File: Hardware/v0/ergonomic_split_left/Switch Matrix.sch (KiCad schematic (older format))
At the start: 86 parts, among them SW100 L41, SW101 L51, SW102 L02, SW103 L12, SW104 L22, SW105 L32, SW106 L42, SW107 L52, SW108 L03, SW109 L13, SW110 L23, SW111 L33, SW112 L43, SW113 L53, SW114 L04, SW115 L14, SW116 L24, SW117 L34, SW118 L44, SW119 L54, SW120 L05, SW121 L15, SW122 L25, SW123 L25, SW124 L55, SW125 L06, SW126 L16, SW127 L36, SW128 L56, SW90 L00, SW91 L10, SW92 L20, SW94 L30, SW95 L40, SW96 L01, SW97 L11, SW98 L21, SW99 L31

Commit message: Switch matrix placement
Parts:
- removed D1, D10, D11, D12, D120, D121, D122, D123, D124, D125, D126, D13, D14, D15, D16, D17, D18, D19, D2, D20, D21, D22, D23, D24, D25, D26, D27, D28, D29, D3, D30, D31, D4, D5, D6, D7, D8, D9: D, custom_footprint_library:SOD323_HS, symbol Device:D
- removed SW100: L41, CherryMX_PCB_KailhSocket:CherryMX_1.00u_PCB_KailhSocket, symbol CherryMX:CherryMX
- removed SW101: L51, CherryMX_PCB_KailhSocket:CherryMX_1.00u_PCB_KailhSocket, symbol CherryMX:CherryMX
- removed SW102: L02, CherryMX_PCB_KailhSocket:CherryMX_1.00u_PCB_KailhSocket, symbol CherryMX:CherryMX
- removed SW103: L12, CherryMX_PCB_KailhSocket:CherryMX_1.00u_PCB_KailhSocket, symbol CherryMX:CherryMX
- removed SW104: L22, CherryMX_PCB_KailhSocket:CherryMX_1.00u_PCB_KailhSocket, symbol CherryMX:CherryMX
- removed SW105: L32, CherryMX_PCB_KailhSocket:CherryMX_1.00u_PCB_KailhSocket, symbol CherryMX:CherryMX
- removed SW106: L42, CherryMX_PCB_KailhSocket:CherryMX_1.00u_PCB_KailhSocket, symbol CherryMX:CherryMX
- removed SW107: L52, CherryMX_PCB_KailhSocket:CherryMX_2.00u_PCB_KailhSocket, symbol CherryMX:CherryMX
- removed SW108: L03, CherryMX_PCB_KailhSocket:CherryMX_1.00u_PCB_KailhSocket, symbol CherryMX:CherryMX
- removed SW109: L13, CherryMX_PCB_KailhSocket:CherryMX_1.00u_PCB_KailhSocket, symbol CherryMX:CherryMX
- removed SW110: L23, CherryMX_PCB_KailhSocket:CherryMX_1.00u_PCB_KailhSocket, symbol CherryMX:CherryMX
- removed SW111: L33, CherryMX_PCB_KailhSocket:CherryMX_1.00u_PCB_KailhSocket, symbol CherryMX:CherryMX
- removed SW112: L43, CherryMX_PCB_KailhSocket:CherryMX_1.00u_PCB_KailhSocket, symbol CherryMX:CherryMX
- removed SW113: L53, CherryMX_PCB_KailhSocket:CherryMX_2.00u_PCB_KailhSocket, symbol CherryMX:CherryMX
- removed SW114: L04, CherryMX_PCB_KailhSocket:CherryMX_1.00u_PCB_KailhSocket, symbol CherryMX:CherryMX
- removed SW115: L14, CherryMX_PCB_KailhSocket:CherryMX_1.00u_PCB_KailhSocket, symbol CherryMX:CherryMX
- removed SW116: L24, CherryMX_PCB_KailhSocket:CherryMX_1.00u_PCB_KailhSocket, symbol CherryMX:CherryMX
- removed SW117: L34, CherryMX_PCB_KailhSocket:CherryMX_1.00u_PCB_KailhSocket, symbol CherryMX:CherryMX
- removed SW118: L44, CherryMX_PCB_KailhSocket:CherryMX_1.00u_PCB_KailhSocket, symbol CherryMX:CherryMX
- removed SW119: L54, CherryMX_PCB_KailhSocket:CherryMX_1.00u_PCB_KailhSocket, symbol CherryMX:CherryMX
- removed SW120: L05, CherryMX_PCB_KailhSocket:CherryMX_1.00u_PCB_KailhSocket, symbol CherryMX:CherryMX
- removed SW121: L15, CherryMX_PCB_KailhSocket:CherryMX_1.00u_PCB_KailhSocket, symbol CherryMX:CherryMX
- removed SW122, SW123: L25, CherryMX_PCB_KailhSocket:CherryMX_1.00u_PCB_KailhSocket, symbol CherryMX:CherryMX
- removed SW124: L55, CherryMX_PCB_KailhSocket:CherryMX_1.00u_PCB_KailhSocket, symbol CherryMX:CherryMX
- removed SW125: L06, CherryMX_PCB_KailhSocket:CherryMX_1.00u_PCB_KailhSocket, symbol CherryMX:CherryMX
- removed SW126: L16, CherryMX_PCB_KailhSocket:CherryMX_1.50u_PCB_KailhSocket, symbol CherryMX:CherryMX
- removed SW127: L36, CherryMX_PCB_KailhSocket:CherryMX_1.50u_PCB_KailhSocket, symbol CherryMX:CherryMX
- removed SW128: L56, CherryMX_PCB_KailhSocket:CherryMX_1.00u_PCB_KailhSocket, symbol CherryMX:CherryMX
- removed SW90: L00, CherryMX_PCB_KailhSocket:CherryMX_1.50u_PCB_KailhSocket, symbol CherryMX:CherryMX
- removed SW91: L10, CherryMX_PCB_KailhSocket:CherryMX_1.50u_PCB_KailhSocket, symbol CherryMX:CherryMX
- removed SW92: L20, CherryMX_PCB_KailhSocket:CherryMX_1.50u_PCB_KailhSocket, symbol CherryMX:CherryMX
- removed SW94: L30, CherryMX_PCB_KailhSocket:CherryMX_1.50u_PCB_KailhSocket, symbol CherryMX:CherryMX
- removed SW95: L40, CherryMX_PCB_KailhSocket:CherryMX_1.50u_PCB_KailhSocket, symbol CherryMX:CherryMX
- removed SW96: L01, CherryMX_PCB_KailhSocket:CherryMX_1.00u_PCB_KailhSocket, symbol CherryMX:CherryMX
- removed SW97: L11, CherryMX_PCB_KailhSocket:CherryMX_1.00u_PCB_KailhSocket, symbol CherryMX:CherryMX
- removed SW98: L21, CherryMX_PCB_KailhSocket:CherryMX_1.00u_PCB_KailhSocket, symbol CherryMX:CherryMX
- removed SW99: L31, CherryMX_PCB_KailhSocket:CherryMX_1.00u_PCB_KailhSocket, symbol CherryMX:CherryMX
- removed SW?: CherryMX_Integrated, symbol custom_parts_library:CherryMX_Integrated
- removed SW?: CherryMX_Integrated_Reversed, symbol custom_parts_library:CherryMX_Integrated_Reversed
- added SW11: L41, custom_footprint_library:CherryMX_1.00u_KailhSocket_Integrated, symbol custom_parts_library:CherryMX_Integrated
- added SW12: L51, custom_footprint_library:CherryMX_1.00u_KailhSocket_Integrated, symbol custom_parts_library:CherryMX_Integrated_Reversed
- added SW13: L02, custom_footprint_library:CherryMX_1.00u_KailhSocket_Integrated, symbol custom_parts_library:CherryMX_Integrated
- added SW14: L12, custom_footprint_library:CherryMX_1.00u_KailhSocket_Integrated_Reversed, symbol custom_parts_library:CherryMX_Integrated_Reversed
- added SW15: L22, custom_footprint_library:CherryMX_1.00u_KailhSocket_Integrated, symbol custom_parts_library:CherryMX_Integrated
- added SW16: L32, custom_footprint_library:CherryMX_1.00u_KailhSocket_Integrated_Reversed, symbol custom_parts_library:CherryMX_Integrated_Reversed
- added SW17: L42, custom_footprint_library:CherryMX_1.00u_KailhSocket_Integrated, symbol custom_parts_library:CherryMX_Integrated
- added SW18: L52, custom_footprint_library:CherryMX_2.00u_KailhSocket_Integrated_Vertical, symbol custom_parts_library:CherryMX_Integrated_Reversed
- added SW19: L03, custom_footprint_library:CherryMX_1.00u_KailhSocket_Integrated, symbol custom_parts_library:CherryMX_Integrated
- added SW20: L13, custom_footprint_library:CherryMX_1.00u_KailhSocket_Integrated_Reversed, symbol custom_parts_library:CherryMX_Integrated_Reversed
- added SW21: L23, custom_footprint_library:CherryMX_1.00u_KailhSocket_Integrated, symbol custom_parts_library:CherryMX_Integrated
- added SW22: L33, custom_footprint_library:CherryMX_1.00u_KailhSocket_Integrated_Reversed, symbol custom_parts_library:CherryMX_Integrated_Reversed
- added SW23: L43, custom_footprint_library:CherryMX_1.00u_KailhSocket_Integrated, symbol custom_parts_library:CherryMX_Integrated
- added SW24: L53, custom_footprint_library:CherryMX_2.00u_KailhSocket_Integrated_Vertical, symbol custom_parts_library:CherryMX_Integrated_Reversed
- added SW25: L04, custom_footprint_library:CherryMX_1.00u_KailhSocket_Integrated, symbol custom_parts_library:CherryMX_Integrated
- added SW26: L14, custom_footprint_library:CherryMX_1.00u_KailhSocket_Integrated_Reversed, symbol custom_parts_library:CherryMX_Integrated_Reversed
- added SW27: L24, custom_footprint_library:CherryMX_1.00u_KailhSocket_Integrated, symbol custom_parts_library:CherryMX_Integrated
- added SW28: L34, custom_footprint_library:CherryMX_1.00u_KailhSocket_Integrated_Reversed, symbol custom_parts_library:CherryMX_Integrated_Reversed
- added SW29: L44, custom_footprint_library:CherryMX_1.00u_KailhSocket_Integrated, symbol custom_parts_library:CherryMX_Integrated
- added SW30: L54, custom_footprint_library:CherryMX_1.00u_KailhSocket_Integrated_Reversed, symbol custom_parts_library:CherryMX_Integrated
- added SW31: L05, custom_footprint_library:CherryMX_1.00u_KailhSocket_Integrated, symbol custom_parts_library:CherryMX_Integrated
- added SW32: L15, custom_footprint_library:CherryMX_1.00u_KailhSocket_Integrated_Reversed, symbol custom_parts_library:CherryMX_Integrated_Reversed
- added SW33: L25, custom_footprint_library:CherryMX_1.00u_KailhSocket_Integrated, symbol custom_parts_library:CherryMX_Integrated
- added SW34: L35, custom_footprint_library:CherryMX_1.00u_KailhSocket_Integrated_Reversed, symbol custom_parts_library:CherryMX_Integrated_Reversed
- added SW35: L55, custom_footprint_library:CherryMX_1.00u_KailhSocket_Integrated_Reversed, symbol custom_parts_library:CherryMX_Integrated_Reversed
- added SW36: L16, custom_footprint_library:CherryMX_1.50u_KailhSocket_Integrated_Vertical_Reversed, symbol custom_parts_library:CherryMX_Integrated_Reversed
- added SW37: L36, custom_footprint_library:CherryMX_1.50u_KailhSocket_Integrated_Vertical_Reversed, symbol custom_parts_library:CherryMX_Integrated_Reversed
- added SW38: L56, custom_footprint_library:CherryMX_1.00u_KailhSocket_Integrated_Reversed, symbol custom_parts_library:CherryMX_Integrated_Reversed
- added SW39: L06, custom_footprint_library:CherryMX_1.00u_KailhSocket_Integrated, symbol custom_parts_library:CherryMX_Integrated
- added SW6: L40, custom_footprint_library:CherryMX_1.50u_KailhSocket_Integrated, symbol custom_parts_library:CherryMX_Integrated
- SW10: renamed from SW?; value CherryMX_Integrated_Reversed -> L31; footprint (none) -> custom_footprint_library:CherryMX_1.00u_KailhSocket_Integrated_Reversed
- SW2: renamed from SW?; value CherryMX_Integrated -> L00; footprint (none) -> custom_footprint_library:CherryMX_1.50u_KailhSocket_Integrated
- SW3: renamed from SW?; value CherryMX_Integrated_Reversed -> L10; footprint (none) -> custom_footprint_library:CherryMX_1.50u_KailhSocket_Integrated_Reversed
- SW4: renamed from SW?; value CherryMX_Integrated -> L20; footprint (none) -> custom_footprint_library:CherryMX_1.50u_KailhSocket_Integrated
- SW5: renamed from SW?; value CherryMX_Integrated_Reversed -> L30; footprint (none) -> custom_footprint_library:CherryMX_1.50u_KailhSocket_Integrated_Reversed
- SW7: renamed from SW?; value CherryMX_Integrated -> L01; footprint (none) -> custom_footprint_library:CherryMX_1.00u_KailhSocket_Integrated
- SW8: renamed from SW?; value CherryMX_Integrated_Reversed -> L11; footprint (none) -> custom_footprint_library:CherryMX_1.00u_KailhSocket_Integrated_Reversed
- SW9: renamed from SW?; value CherryMX_Integrated -> L21; footprint (none) -> custom_footprint_library:CherryMX_1.00u_KailhSocket_Integrated
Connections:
- net labels added: RGB_DIN, RGB_DOUT, RGB_L44, RGB_L51, RGB_L54, RGB_L55, ROW[5]
- wire segments 411 -> 738
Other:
- moved on the sheet: SW10, SW2, SW3, SW4, SW5, SW7, SW8, SW9

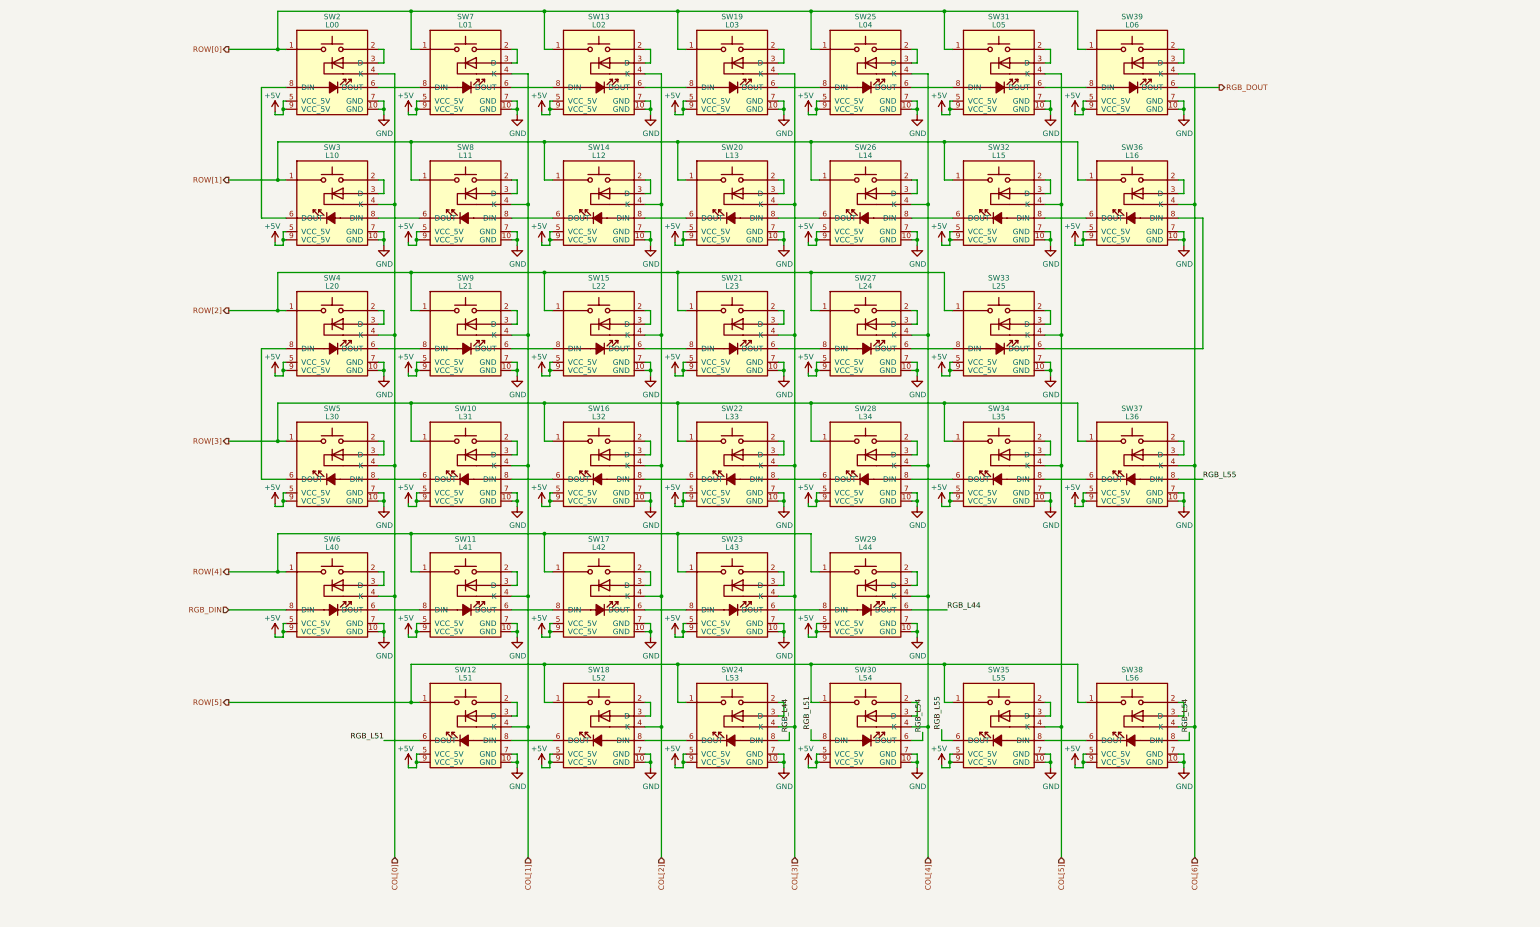
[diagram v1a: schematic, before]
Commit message: Connecting schematic blocks, most sub-blocks done
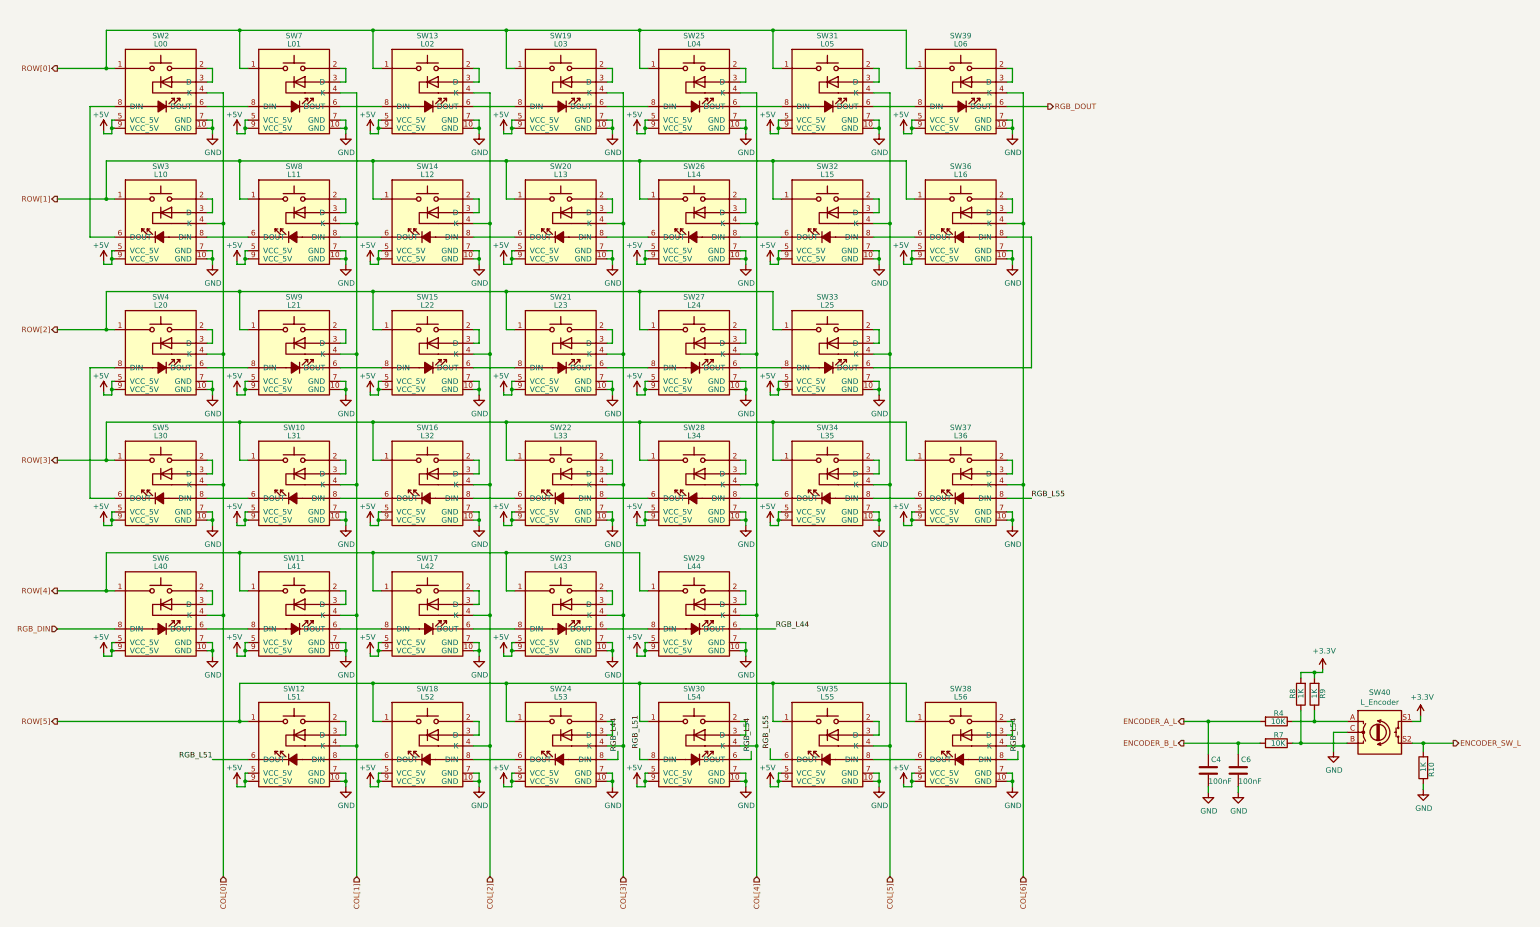
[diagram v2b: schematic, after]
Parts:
- added C4, C6: 100nF, Capacitor_smd:C_0603_1608Metric, symbol Device:C
- added R10, R8, R9: 1K, resistor_smd:R_0603_1608Metric, symbol Device:R
- added R4, R7: 10K, resistor_smd:R_0603_1608Metric, symbol Device:R
- added SW40: L_Encoder, Rotary_Encoder:RotaryEncoder_Alps_EC11E-Switch_Vertical_H20mm, symbol Device:Rotary_Encoder_Switch
- SW10, SW14, SW16, SW20, SW22, SW26, SW28, SW30, SW32, SW34, SW35, SW38, SW8: footprint custom_footprint_library:CherryMX_1.00u_KailhSocket_Integrated_Reversed -> custom_footprint_library:CherryMX_1.00u_KailhSocket_Integrated
- SW11, SW12, SW13, SW15, SW17, SW19, SW21, SW23, SW25, SW27, SW29, SW31, SW33, SW39, SW7, SW9: footprint custom_footprint_library:CherryMX_1.00u_KailhSocket_Integrated -> custom_footprint_library:CherryMX_1.00u_KailhSocket_Integrated_Reversed
- SW18, SW24: footprint custom_footprint_library:CherryMX_2.00u_KailhSocket_Integrated_Vertical -> custom_footprint_library:CherryMX_2.00u_KailhSocket_Integrated_Vertical_Reversed
- SW2, SW4, SW6: footprint custom_footprint_library:CherryMX_1.50u_KailhSocket_Integrated -> custom_footprint_library:CherryMX_1.50u_KailhSocket_Integrated_Reversed
- SW3, SW5: footprint custom_footprint_library:CherryMX_1.50u_KailhSocket_Integrated_Reversed -> custom_footprint_library:CherryMX_1.50u_KailhSocket_Integrated
- SW36, SW37: footprint custom_footprint_library:CherryMX_1.50u_KailhSocket_Integrated_Vertical_Reversed -> custom_footprint_library:CherryMX_1.50u_KailhSocket_Integrated_Vertical
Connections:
- net GND: now also C4.2, C6.2, R10.1, SW40.C
- new net: R4.1, R9.1, SW40.A
- new net: R7.1, R8.1, SW40.B
- new net +3V3: R8.2, R9.2, SW40.S1
- new net ENCODER_A_L: C4.1, R4.2
- new net ENCODER_B_L: C6.1, R7.2
- new net ENCODER_SW_L: R10.2, SW40.S2
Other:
- moved on the sheet: SW10, SW11, SW12, SW13, SW14, SW15, SW16, SW17, SW18, SW19, SW2, SW20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

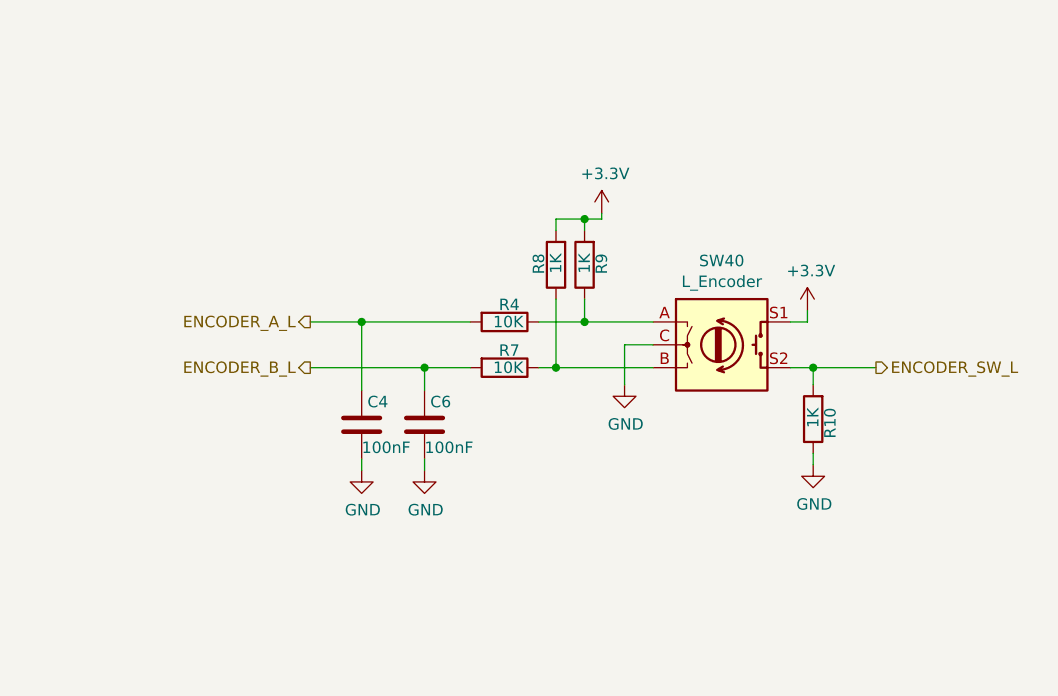
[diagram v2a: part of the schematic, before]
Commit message: Drawing board outline Basic placement done Adding rotary encoder to the switch matrix Adding mounting holes
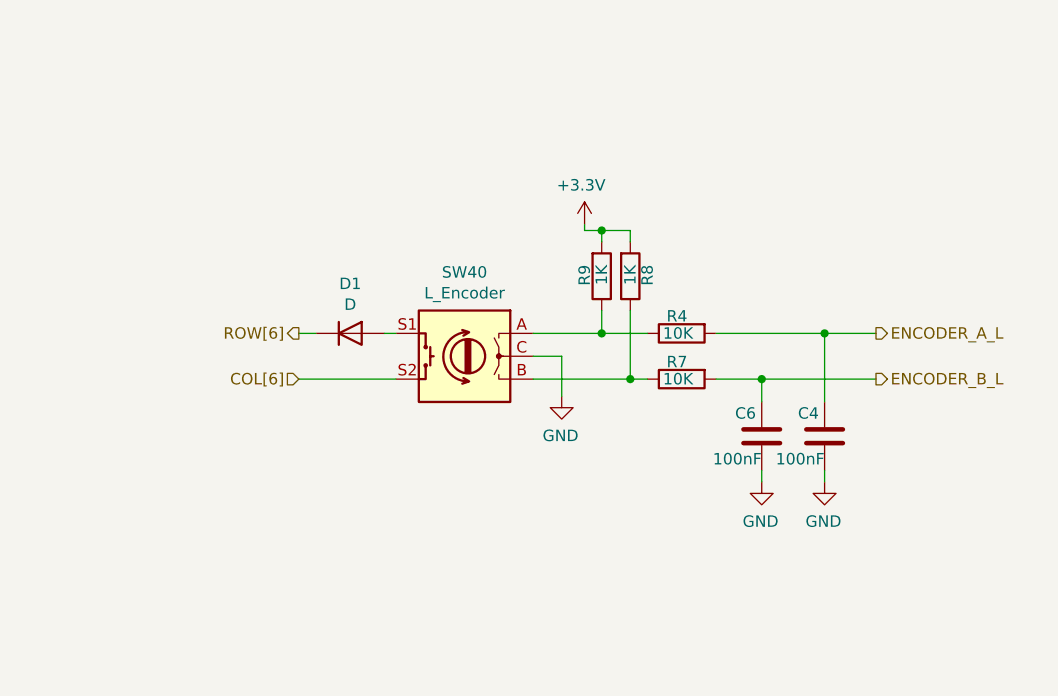
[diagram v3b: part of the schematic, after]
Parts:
- removed R10: 1K, resistor_smd:R_0603_1608Metric, symbol Device:R
- added D1: D, custom_footprint_library:SOD323_HS, symbol Device:D
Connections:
- net ENCODER_SW_L is gone; now on net COL[6]: SW40.S2
- net +3V3: no longer SW40.S1
- new net: D1.2 (A), SW40.S1
- new net ROW[6]: D1.1 (K)
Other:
- moved on the sheet: C4, C6, R4, R7, R8, R9, SW40

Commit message: Adding power and ground planes Adding right interface USB C connector Pin swapping on ATMEGA
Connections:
- net COL[6]: now also D1.1 (K); no longer SW40.S2
- net ROW[6]: now also SW40.S1; no longer D1.1 (K)
- net at D1.2 (A): now also SW40.S2; no longer SW40.S1
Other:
- moved on the sheet: D1
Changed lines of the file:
@@
 L Device:D D1
 U 1 1 62BFACFD
-P 12575 8400
-F 0 "D1" H 12575 8617 50  0000 C CNN
-F 1 "D" H 12575 8526 50  0000 C CNN
-F 2 "custom_footprint_library:SOD323_HS" H 12575 8400 50  0001 C CNN
-F 3 "~" H 12575 8400 50  0001 C CNN
-	1    12575 8400
+P 12575 8600
+F 0 "D1" H 12550 8500 50  0000 C CNN
+F 1 "D" H 12675 8550 50  0000 C CNN
+F 2 "custom_footprint_library:SOD323_HS" H 12575 8600 50  0001 C CNN
+F 3 "~" H 12575 8600 50  0001 C CNN
+	1    12575 8600
 	1    0    0    -1
 $EndComp
 Wire Wire Line
-	12725 8400 12775 8400
+	12725 8600 12775 8600
 Text HLabel 12350 8400 0    50   Output ~ 0
 ROW[6]
 Wire Wire Line
-	12350 8400 12425 8400
+	12350 8600 12425 8600
 Wire Wire Line
-	12350 8600 12775 8600
+	12350 8400 12775 8400
 $EndSCHEMATC

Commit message: Debug connectors Adding I2C debug header Changed SPI programming header to edge mount Changed right interface connector to IDC Cleaning up schematic
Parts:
- SW6: footprint custom_footprint_library:CherryMX_1.50u_KailhSocket_Integrated_Reversed -> custom_footprint_library:CherryMX_1.00u_KailhSocket_Integrated_Reversed
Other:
- note added: "Rotary Encoder"
- note added: "Switch Matrix"
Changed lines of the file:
@@
 F 0 "SW6" H 3000 7800 50  0000 C CNN
 F 1 "L40" H 3000 7725 50  0000 C CNN
-F 2 "custom_footprint_library:CherryMX_1.50u_KailhSocket_Integrated_Reversed" H 3000 7325 50  0001 C CNN
+F 2 "custom_footprint_library:CherryMX_1.00u_KailhSocket_Integrated_Reversed" H 3000 7325 50  0001 C CNN
 F 3 "" H 3000 7325 50  0001 C CNN
 	1    3000 7325
@@
 Wire Wire Line
 	12350 8400 12775 8400
+Text Notes 750  1000 0    315  ~ 0
+Switch Matrix
+Wire Notes Line
+	1500 10500 11750 10500
+Wire Notes Line
+	11750 1500 11750 10500
+Wire Notes Line
+	1500 1500 1500 10500
+Wire Notes Line
+	1500 1500 11750 1500
+Wire Notes Line
+	15500 7500 12000 7500
+Wire Notes Line
+	12000 7500 12000 9500
+Wire Notes Line
+	12000 9500 15500 9500
+Wire Notes Line
+	15500 7500 15500 9500
+Text Notes 1525 1600 0    50   ~ 0
+Switch Matrix
+Text Notes 12025 7600 0    50   ~ 0
+Rotary Encoder
 $EndSCHEMATC
